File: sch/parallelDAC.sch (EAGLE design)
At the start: 34 parts, among them IC1 AD558, IC2 LM324N, IC3 AD7819, IC4 LM555N, X1 1802 Membership Card GPIO

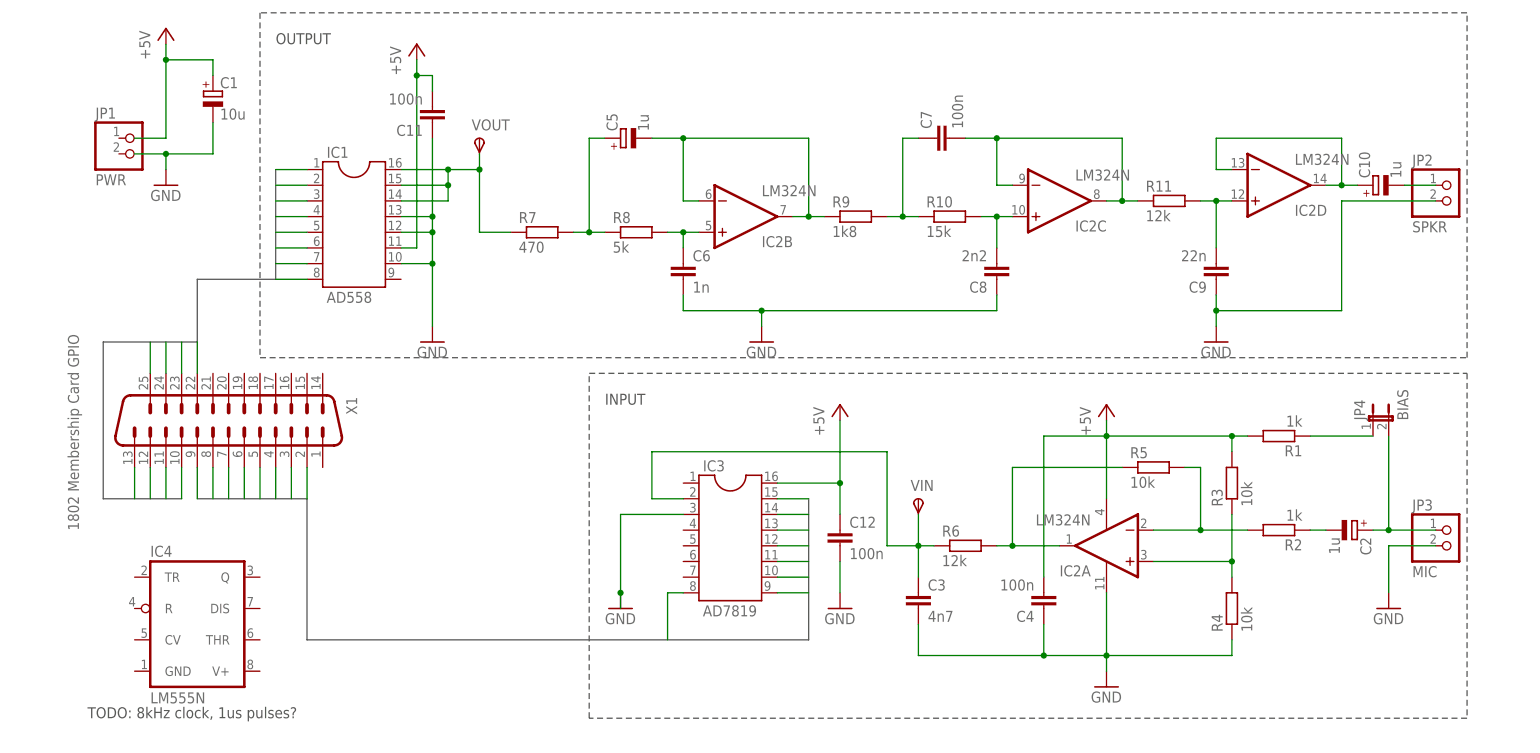
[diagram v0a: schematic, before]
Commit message: 8kHz HW clock, or maybe using SW and just tuning the CPU clock?
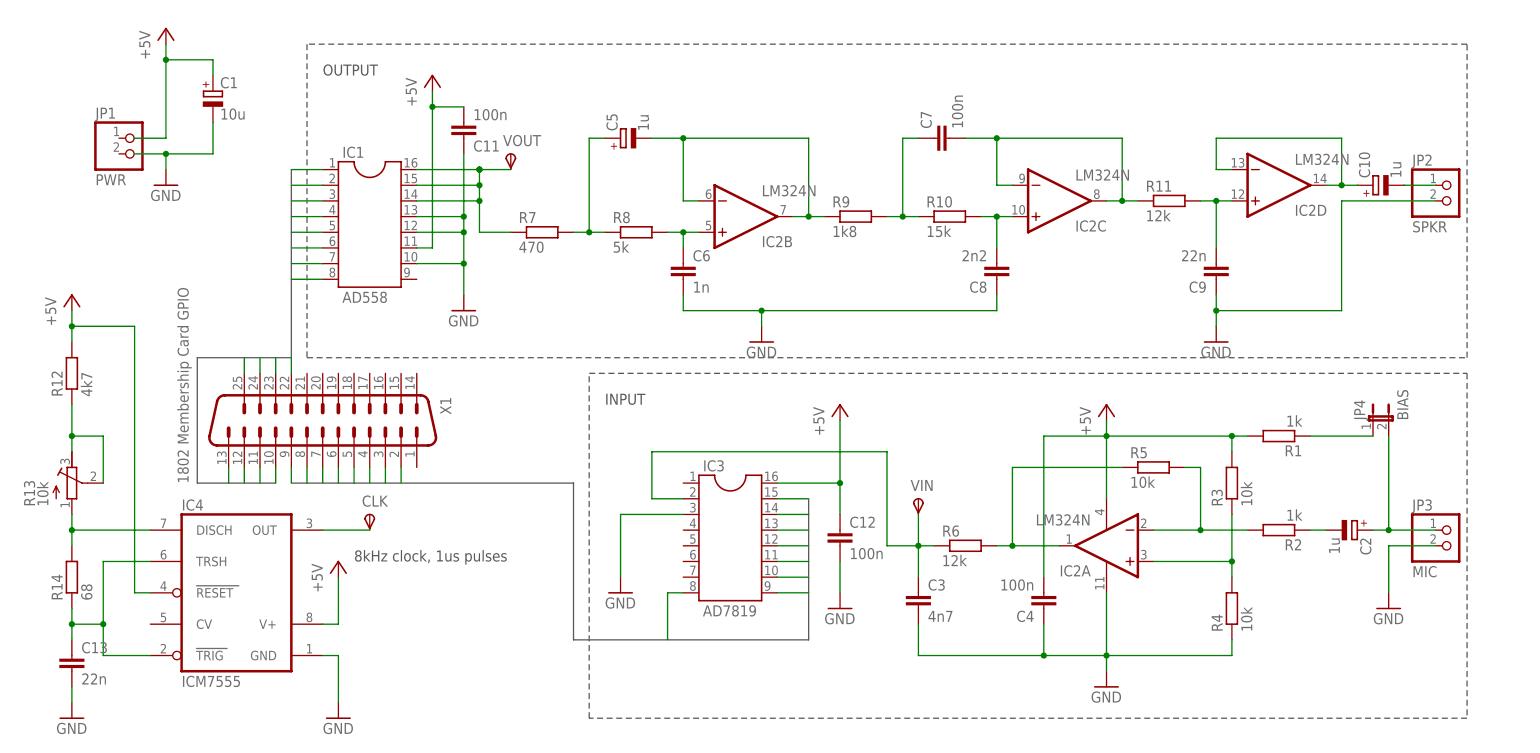
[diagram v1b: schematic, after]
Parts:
- added C13: 22n, resistor:C-EU025-024X044
- added CLK: TPSPAD1-13, testpad:TPSPAD1-13
- added R12: 4k7, resistor:R-EU_0207/2V
- added R13: 10k, rcl:R-TRIMM64W
- added R14: 68, resistor:R-EU_0207/2V
- IC4: value LM555N -> ICM7555; device linear:LM555N -> maxim:ICM7555
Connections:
- new net N$17: R12.1, R13.E, R13.S
- new net N$19: IC4.DISCH, R13.A, R14.2
- new net N$20: C13.1, IC4.TRIG, IC4.TRSH, R14.1
- new net N$21: CLK.PP, IC4.OUT
- net +5V: now also IC4.RESET, IC4.V+, R12.2
- net GND: now also C13.2, IC4.GND
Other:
- note added: "8kHz clock, 1us pulses"
- note removed: "TODO: 8kHz clock, 1us pulses?"
- moved on the sheet: C11, IC1, VOUT, X1

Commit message: HW sample clock by 555 timer
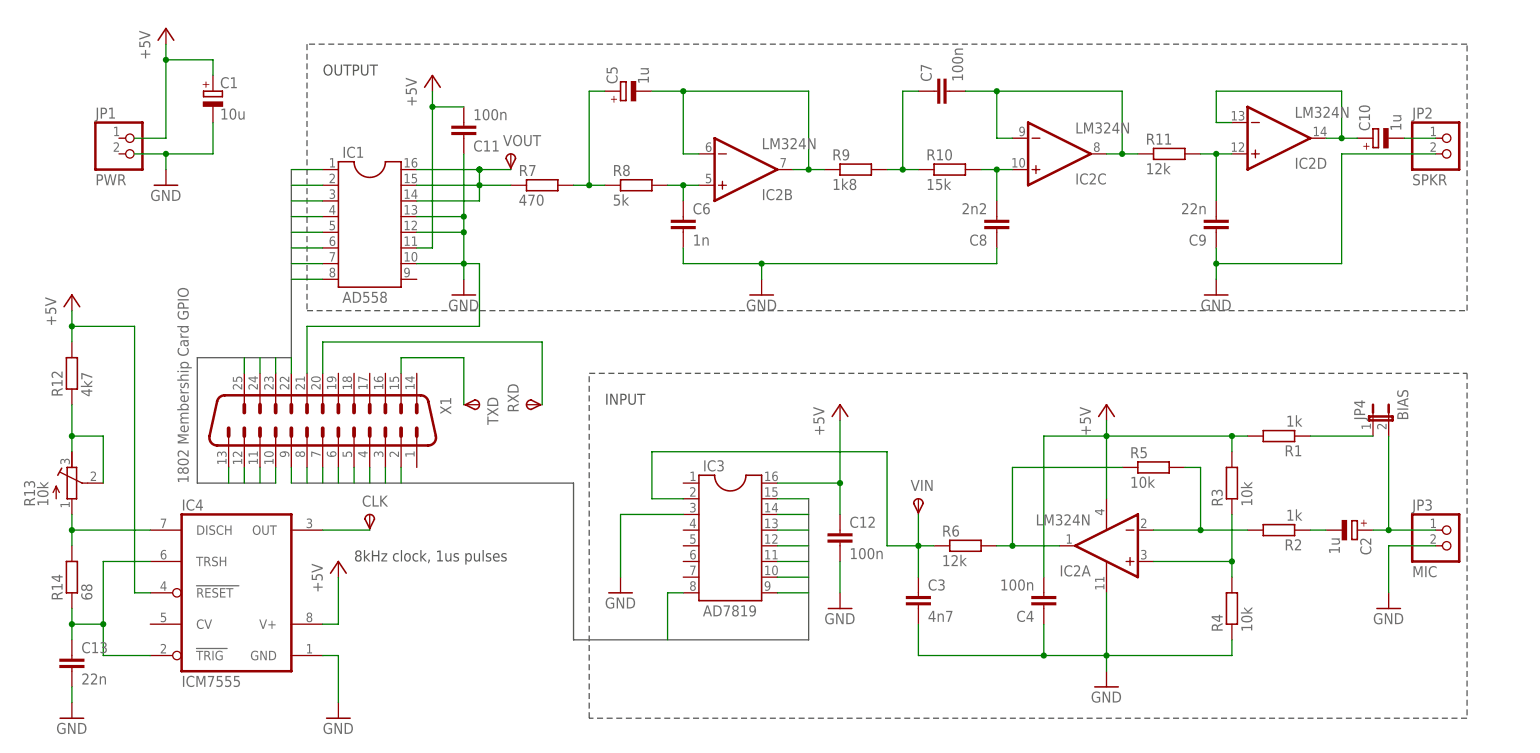
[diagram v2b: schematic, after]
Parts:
- added RXD, TXD: TPSPAD1-13, testpad:TPSPAD1-13
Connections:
- new net N$23: RXD.PP, X1.20
- new net N$24: TXD.PP, X1.15
- net GND: now also X1.21
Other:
- moved on the sheet: C10, C5, C6, C7, C8, C9, IC2B, IC2C, IC2D, JP2, R10, R11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

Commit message: HW sample clock with delay / pulse width (even less SW control for ADC?)
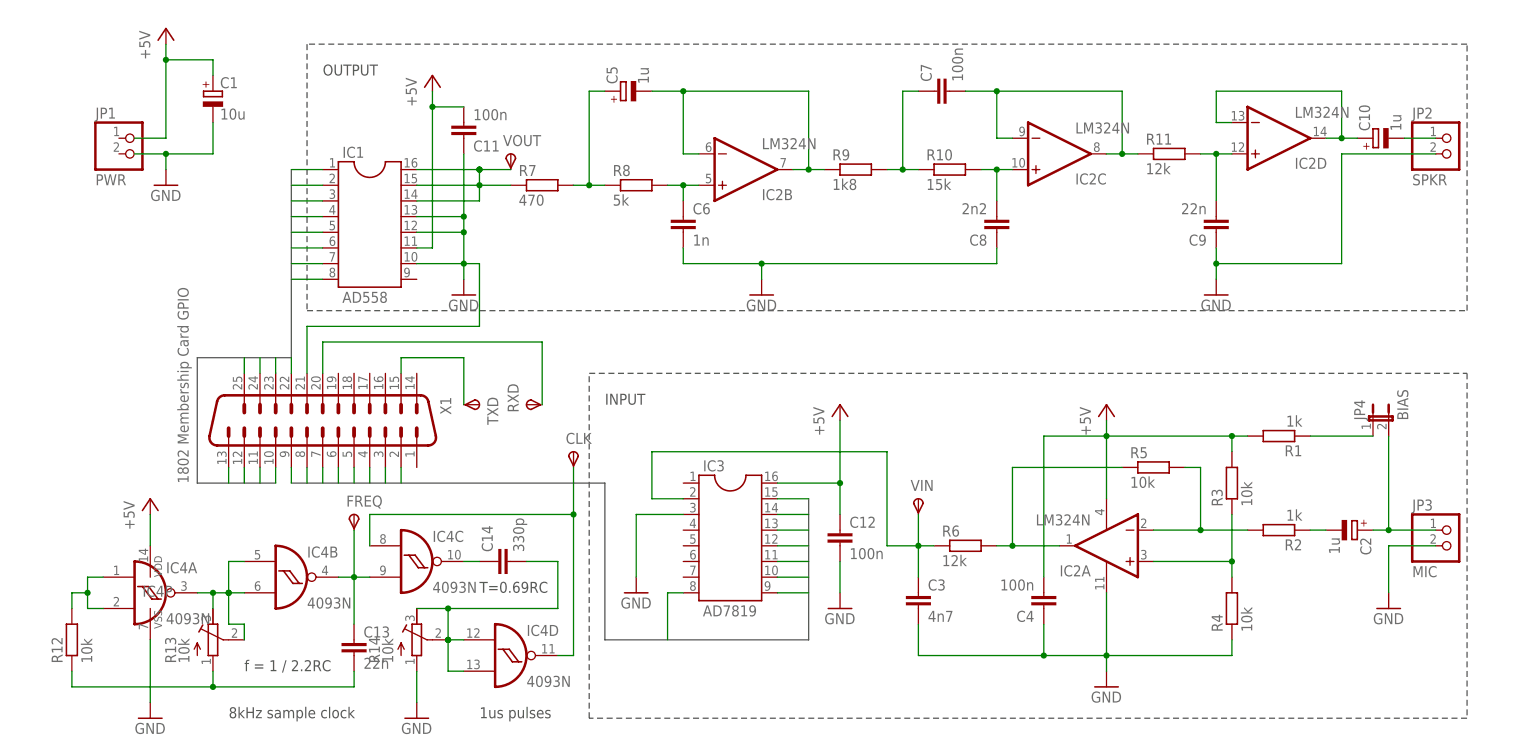
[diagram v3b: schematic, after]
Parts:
- added C14: 330p, resistor:C-EU025-024X044
- added FREQ: TPSPAD1-13, testpad:TPSPAD1-13
- IC4: value ICM7555 -> 4093N; device maxim:ICM7555 -> 40xx:4093N
- R12: value 4k7 -> 10k
- R14: value 68 -> 10k; device resistor:R-EU_0207/2V -> rcl:R-TRIMM64W
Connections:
- new net N$22: C13.1, FREQ.PP, IC4B.O, IC4C.I1
- new net N$26: C14.1, IC4C.O
- new net N$27: CLK.PP, IC4C.I0, IC4D.O
- net +5V: now also IC4P.VDD; no longer IC4.RESET, IC4.V+, R12.2
- net GND: now also IC4P.VSS, R14.A; no longer C13.2, IC4.GND
- net N$17: now also IC4A.I0, IC4A.I1, R12.2; no longer R12.1, R13.E, R13.S
- net N$19: now also C13.2, R12.1; no longer IC4.DISCH, R14.2
- net N$20: now also IC4A.O, IC4B.I0, IC4B.I1, R13.E, R13.S; no longer C13.1, IC4.TRIG, IC4.TRSH, R14.1
- net N$21: now also C14.2, IC4D.I0, IC4D.I1, R14.E, R14.S; no longer CLK.PP, IC4.OUT
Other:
- note added: "1us pulses"
- note added: "8kHz sample clock"
- note added: "T=0.69RC"
- note added: "f = 1 / 2.2RC"
- note removed: "8kHz clock, 1us pulses"
- moved on the sheet: C13, CLK, R12, R13

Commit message: Breadboard prototype of sample clock: voltage regularization still missing
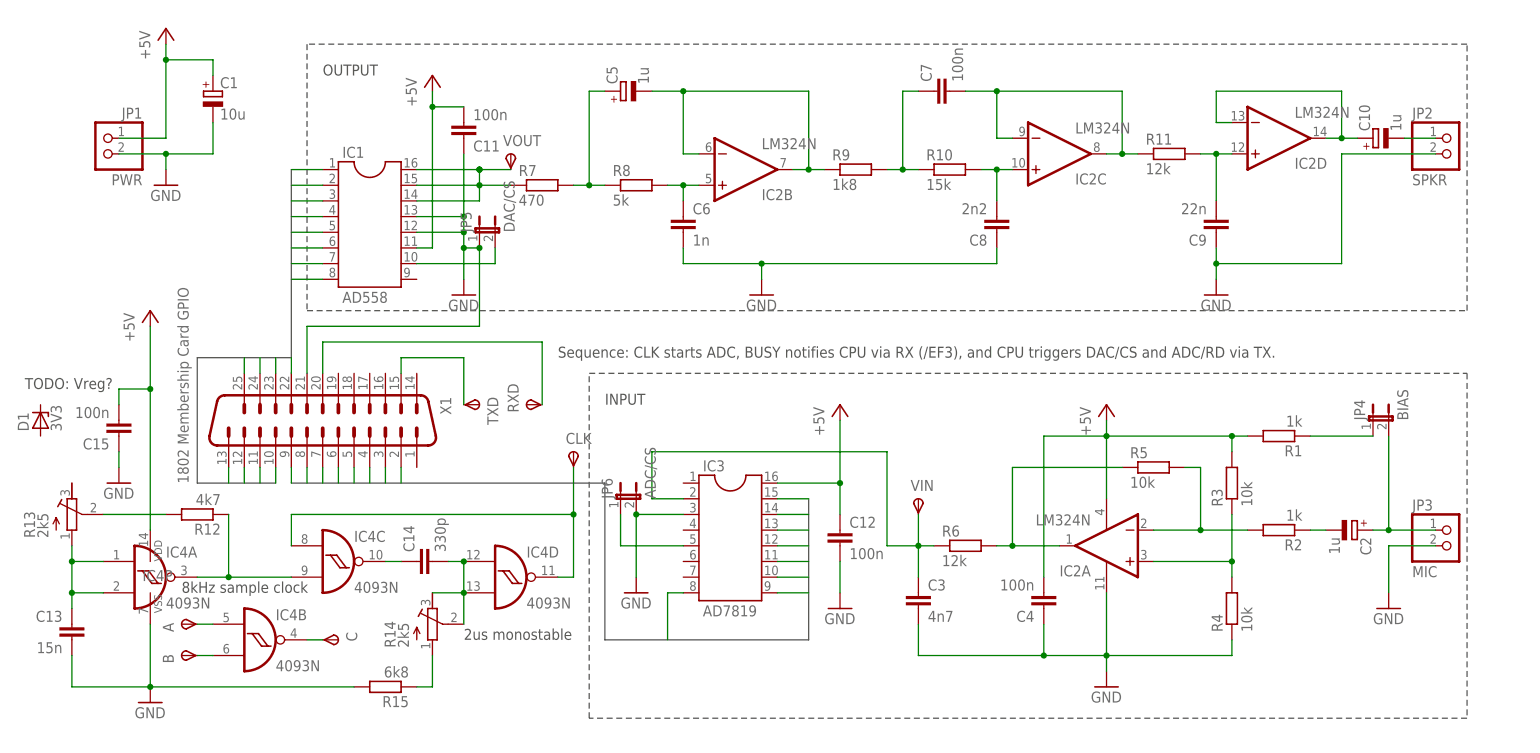
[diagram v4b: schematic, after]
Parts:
- removed FREQ: TPSPAD1-13, testpad:TPSPAD1-13
- added A, B, C: TPSPAD1-13, testpad:TPSPAD1-13
- added C15: 100n, resistor:C-EU025-024X044
- added D1: 3V3, diode:ZENER-DIODEZD-2.5
- added JP5: DAC/CS, jumper:JP1E
- added JP6: ADC/CS, jumper:JP1E
- added R15: 6k8, resistor:R-EU_0207/2V
- C13: value 22n -> 15n
- R12: value 10k -> 4k7
- R13, R14: value 10k -> 2k5
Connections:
- new net N$25: IC3.5, JP6.1
- new net N$28: IC1.10, JP5.2
- new net N$29: R14.A, R15.1
- new net N$30: B.PP, IC4B.I1
- new net N$31: C.PP, IC4B.O
- net +5V: now also C15.2, JP1.1
- net GND: now also C13.2, C15.1, JP1.2, JP5.1, JP6.2, R15.2; no longer IC1.10, R14.A
- net N$17: now also C13.1, R13.A; no longer R12.2
- net N$19: now also R12.2, R13.S; no longer C13.2, R12.1, R13.A
- net N$20: now also A.PP; no longer IC4A.O, IC4B.I1, R13.E, R13.S
- net N$22: now also IC4A.O, R12.1; no longer C13.1, FREQ.PP, IC4B.O
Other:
- note added: "2us monostable"
- note added: "Sequence: CLK starts ADC, BUSY notifies CPU via RX (/EF3), and CPU triggers DAC/CS and ADC/RD via TX."
- note added: "TODO: Vreg?"
- note removed: "1us pulses"
- note removed: "T=0.69RC"
- note removed: "f = 1 / 2.2RC"
- moved on the sheet: C13, C14, IC4A, IC4B, IC4C, IC4D, IC4P, R12, R13, R14
